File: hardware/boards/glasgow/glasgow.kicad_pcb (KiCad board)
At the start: 4 copper layers, 80 x 49 mm, 240 parts, among them J1 USB_B_Micro, J10 Conn_01x03, J2 Conn_02x10_Odd_Even, J3 Conn_02x10_Odd_Even, J4 Conn_01x02, J5 Conn_02x22_Odd_Even, J6 Conn_01x08, J7 Conn_01x08, J8 Conn_01x08, J9 Conn_01x08, U1 CY7C68013A-56LTX, U10 SN74LVC1T45DRL, U11 SN74LVC1T45DRL, U12 ADC081C021CIMM, U13 DAC081C081CIMK, U14 TPS73101DBV, U15 TPD3S014, U16 SN74LVC1T45DRL, U17 SN74LVC1T45DRL, U18 SN74LVC1T45DRL, U19 PCA6408APW, U2 CAT24M01W, U20 DAC081C081CIMK, U21 ADC081C021CIMM, U22 SN74LVC1T45DRL, U23 SN74LVC1T45DRL, U24 SN74LVC1T45DRL, U25 SN74LVC1T45DRL, U26 SN74LVC1T45DRL, U27 SN74LVC1T45DRL, U28 SN74LVC1T45DRL, U29 SN74LVC1T45DRL, U3 CAT24C256W, U30 ICE40HX8K-BG121, U31 TPS73101DBV, U32 SN74LVC1T45DRL, U33 MG2040, U34 ATECC508A, U35 MG2040, U36 TLV73312PQDRVRQ1, U4 SN74LVC1T45DRL, U5 PCA6408APW, U6 SN74LVC1T45DRL, U7 LM3880MF-1AF, U8 TLV75533PDRVR, U9 SN74LVC1T45DRL, Y1 24M

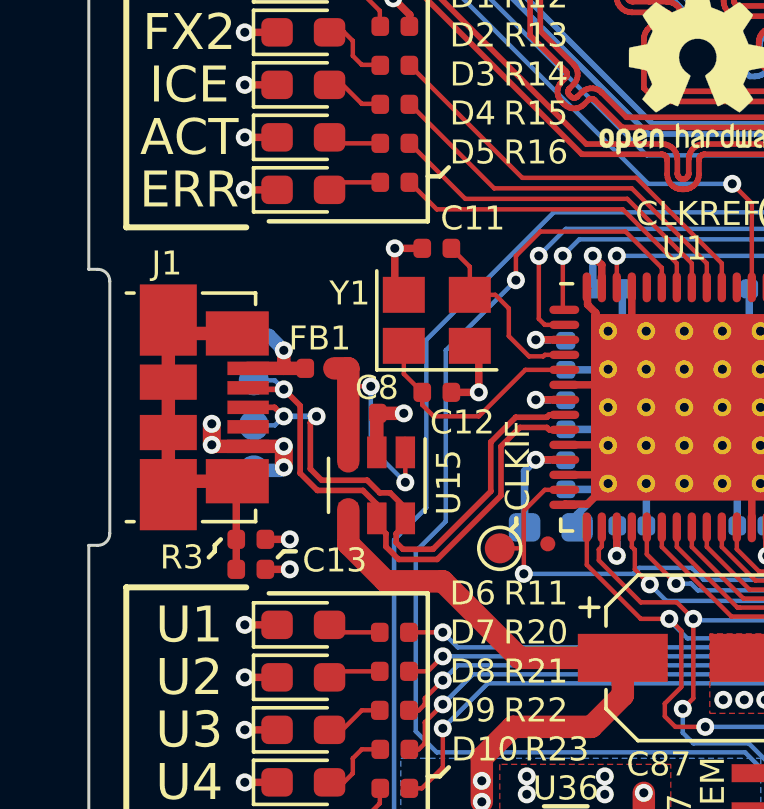
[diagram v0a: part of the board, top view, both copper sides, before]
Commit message: revC1-usbc: changed usb micro connector to usb type C
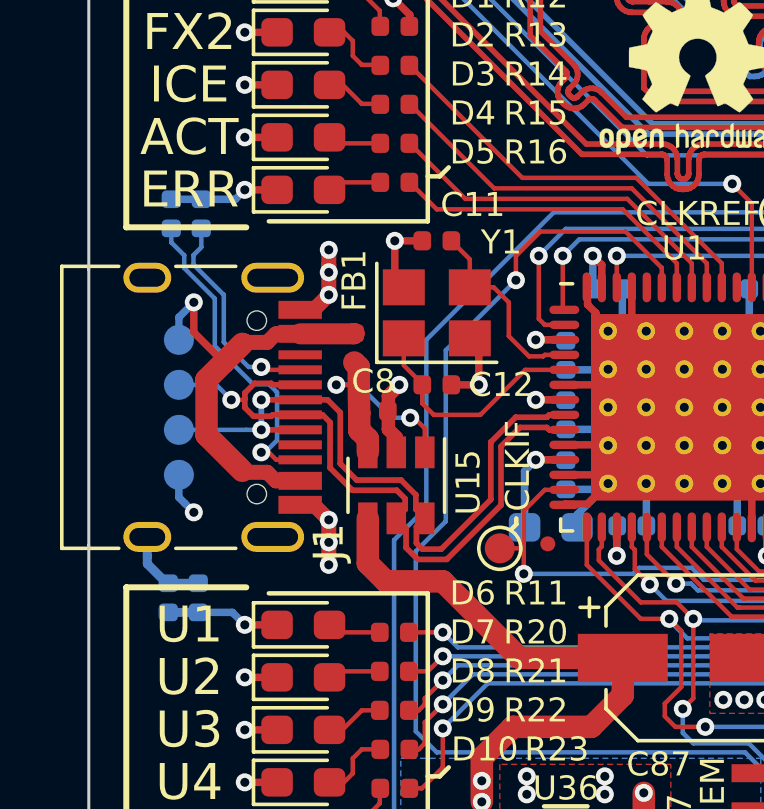
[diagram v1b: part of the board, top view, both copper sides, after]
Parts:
- added R52: 5k11, Resistor_SMD:R_0402_1005Metric, B.Cu at (53.8, 89.0)
- added R53: 5k11, Resistor_SMD:R_0402_1005Metric, B.Cu at (52.8, 89.0)
- C13, R3: moved to B.Cu
- J1: value USB_B_Micro -> USB_C_Receptacle_USB2.0; footprint Connector_USB:USB_Micro-B_Molex_47346-0001 -> Connector_USB:USB_C_Receptacle_HRO_TYPE-C-31-M-12
- moved R3 3.37 mm to (52.6, 101.8), turned to 270 degrees
- moved TP13 2.50 mm to (53.0, 93.3)
- moved TP14 2.50 mm to (53.0, 97.8)
- moved TP15 2.50 mm to (53.0, 96.3)
- moved TP16 2.50 mm to (53.0, 94.8)
- moved C13 1.99 mm to (53.6, 101.8), turned to 270 degrees
- moved FB1 1.34 mm to (58.9, 93.5), turned to 270 degrees
- moved J1 0.85 mm to (53.0, 95.5)
- moved U15 0.65 mm to (60.2, 98.1)
- moved C8 0.34 mm to (59.5, 95.6)
- moved C11 0.25 mm to (61.6, 90.0)
- moved C12 0.25 mm to (61.6, 94.8)
- moved Y1 0.25 mm to (61.6, 92.3)
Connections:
- FB1 pad 1: Net-(FB1-Pad1) -> /VUSBIN
- TP13 pad 1: Net-(FB1-Pad1) -> /VUSBIN
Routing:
- net /VUSBIN: track 0.00 -> 15.7 mm, vias 0 -> 1
- net /SHLD: track 15.1 -> 3.68 mm
- net /USB_CC2: track 0.00 -> 10.9 mm, vias 0 -> 1
- net /USB_CC1: track 0.00 -> 7.25 mm, vias 0 -> 1
- net GND: track 262.0 -> 267.1 mm, vias 116 -> 117
- net /USB_N: track 18.7 -> 22.8 mm
- net Net-(FB1-Pad1): track 3.71 -> 0.00 mm, vias 1 -> 0
- net /USB_P: track 18.9 -> 22.3 mm
- net /VUSB: track 9.50 -> 8.35 mm
- net +5V: track 167.8 -> 167.2 mm
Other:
- outline, holes or cut-outs redrawn

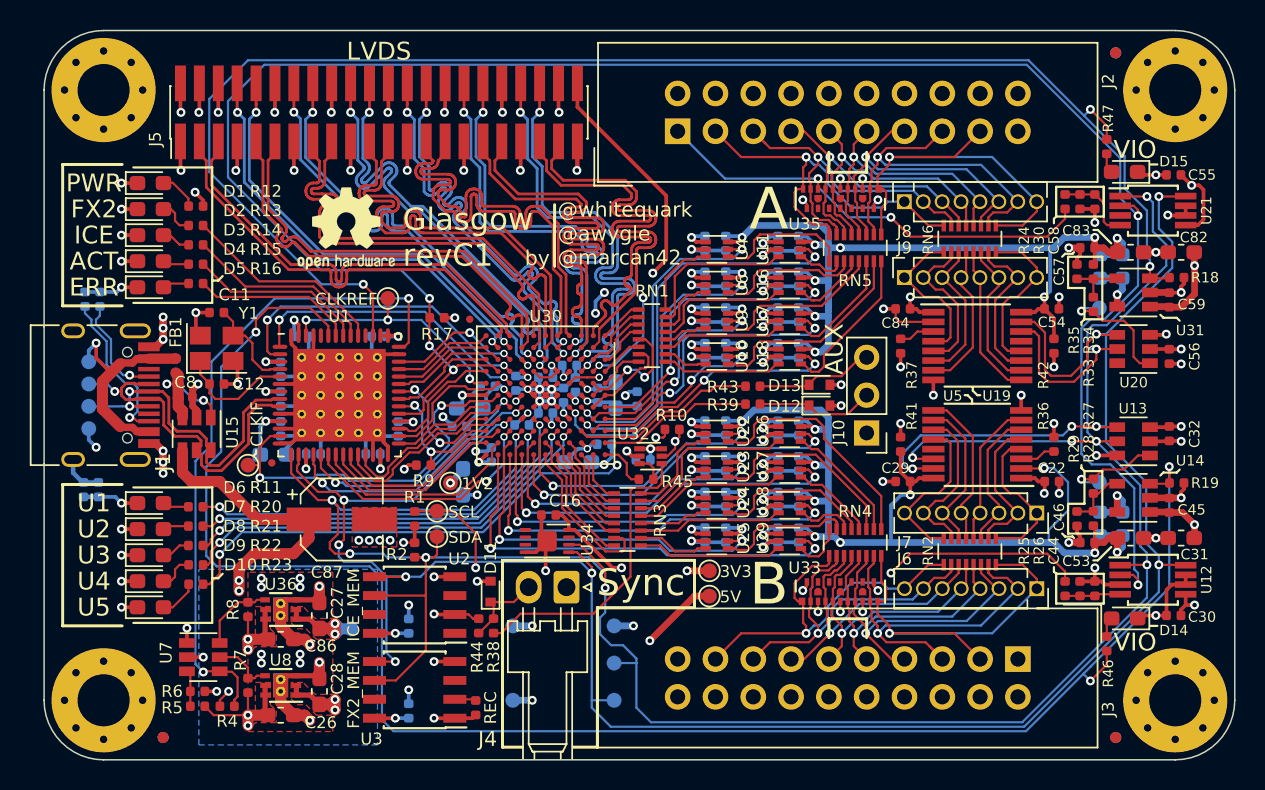
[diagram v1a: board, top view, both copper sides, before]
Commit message: changed level shifters, passing DRC
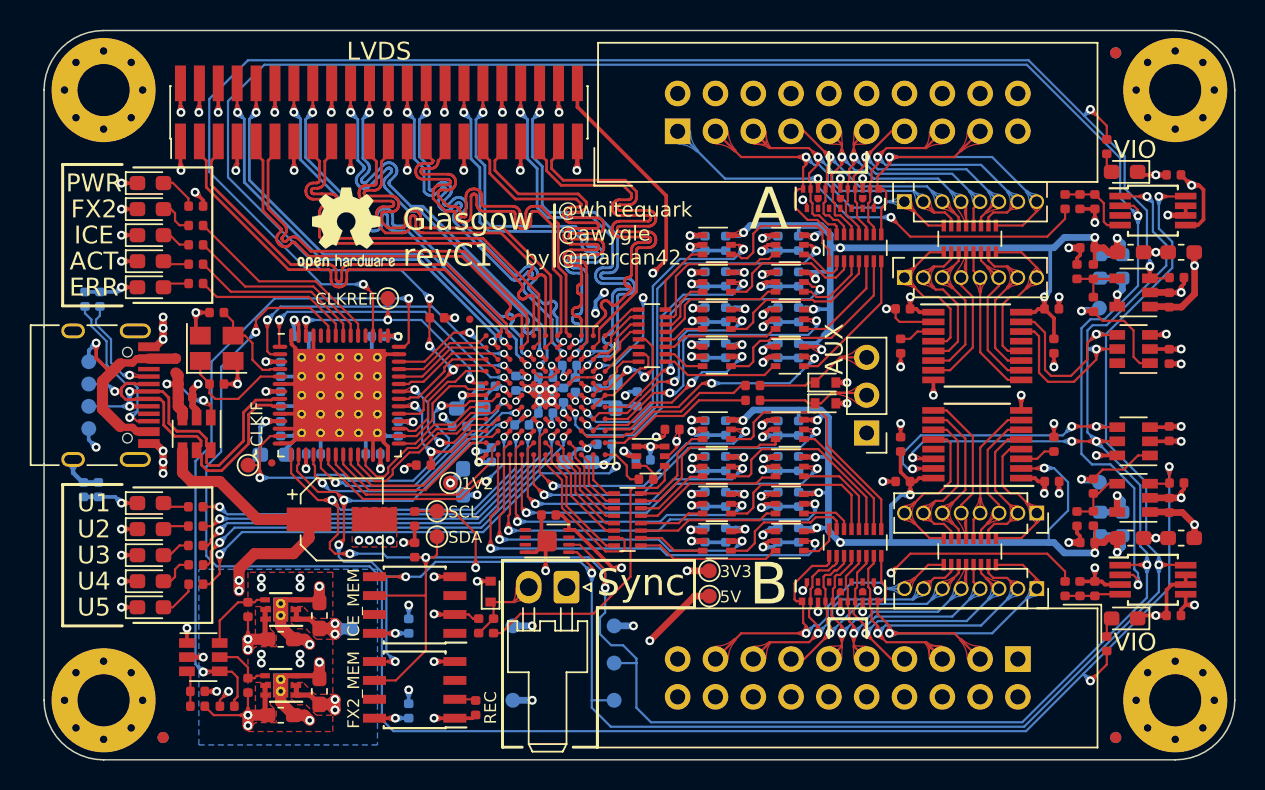
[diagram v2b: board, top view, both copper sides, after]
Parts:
- R52, R53: value 5k11 -> 5K1
- U10, U11, U16, U17, U18, U22, U23, U24, U25, U26, U27, U28, U29, U32, U4, U6, U9: footprint Glasgow:SOT-563 -> Package_TO_SOT_SMD:SOT-363_SC-70-6
- moved D12 0.43 mm to (102.5, 96.0)
- moved D13 0.43 mm to (102.5, 94.7)
- moved U11 0.30 mm to (100.1, 85.4)
- moved U22 0.30 mm to (95.2, 97.8)
- moved U26 0.30 mm to (100.1, 97.8)
- moved U4 0.30 mm to (95.2, 85.4)
- moved R39 0.25 mm to (97.6, 95.8)
- moved U23 0.20 mm to (95.2, 100.3)
- moved U27 0.20 mm to (100.1, 100.3)
- moved U16 0.20 mm to (100.1, 87.9)
- moved U6 0.20 mm to (95.2, 87.9)
- moved U24 0.10 mm to (95.2, 102.8)
- moved U28 0.10 mm to (100.1, 102.8)
- moved U17 0.10 mm to (100.1, 90.4)
- moved U9 0.10 mm to (95.2, 90.4)
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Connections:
- J1 pad A8: Net-(J1-PadA8) -> (no net)
- J1 pad B8: Net-(J1-PadB8) -> (no net)
- J2 pad 19: Net-(J2-Pad19) -> (no net)
- J2 pad 20: Net-(J2-Pad20) -> (no net)
- J3 pad 19: Net-(J3-Pad19) -> (no net)
- J3 pad 20: Net-(J3-Pad20) -> (no net)
- U1 pad 46: Net-(U1-Pad46) -> (no net)
- U1 pad 52: Net-(U1-Pad52) -> (no net)
- U19 pad 13: Net-(U19-Pad13) -> (no net)
- U2 pad 1: Net-(U2-Pad1) -> (no net)
- U2 pad 3: Net-(U2-Pad3) -> (no net)
- U2 pad 7: Net-(U2-Pad7) -> (no net)
- U20 pad 6: /IO_Banks/IO_Buffer_A/ADRDAC -> (no net)
- U21 pad 3: /IO_Banks/IO_Buffer_A/ADRADC -> (no net)
- U3 pad 3: Net-(U3-Pad3) -> (no net)
- U3 pad 7: Net-(U3-Pad7) -> (no net)
- U30 pad B10: Net-(U30-PadB10) -> (no net)
- U33 pad 13: Net-(U33-Pad13) -> (no net)
- U33 pad 14: Net-(U33-Pad14) -> (no net)
- U33 pad 15: Net-(U33-Pad15) -> (no net)
- U33 pad 16: Net-(U33-Pad16) -> (no net)
- U33 pad 17: Net-(U33-Pad17) -> (no net)
- U33 pad 19: Net-(U33-Pad19) -> (no net)
- U33 pad 20: Net-(U33-Pad20) -> (no net)
- U33 pad 21: Net-(U33-Pad21) -> (no net)
- U35 pad 13: Net-(U35-Pad13) -> (no net)
- U35 pad 14: Net-(U35-Pad14) -> (no net)
- U35 pad 15: Net-(U35-Pad15) -> (no net)
- U35 pad 16: Net-(U35-Pad16) -> (no net)
- U35 pad 17: Net-(U35-Pad17) -> (no net)
- U35 pad 19: Net-(U35-Pad19) -> (no net)
- U35 pad 20: Net-(U35-Pad20) -> (no net)
- U35 pad 21: Net-(U35-Pad21) -> (no net)
- U5 pad 13: Net-(U5-Pad13) -> (no net)
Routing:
- net +3V3: track 115.5 -> 112.3 mm
- net /IO_Banks/VIOB: track 114.0 -> 111.2 mm
- net GND: track 267.1 -> 265.1 mm
- net /IO_Banks/VIOA: track 103.6 -> 102.0 mm
- net /IO_Banks/IO_Buffer_B/Y4: track 10.8 -> 12.1 mm
- net /IO_Banks/IO_Buffer_A/Y0: track 9.26 -> 10.2 mm
- net /IO_Banks/IO_Buffer_B/Y7: track 3.71 -> 2.78 mm
- net /IO_Banks/IO_Buffer_B/Y3: track 5.64 -> 6.48 mm
- net /IO_Banks/IO_Buffer_A/Y7: track 10.6 -> 9.76 mm
- net /IO_Banks/IO_Buffer_A/Y5: track 7.77 -> 7.15 mm
- net /IO_Banks/DA3: track 20.7 -> 21.3 mm
- net /IO_Banks/IO_Buffer_B/Y0: track 16.3 -> 16.9 mm

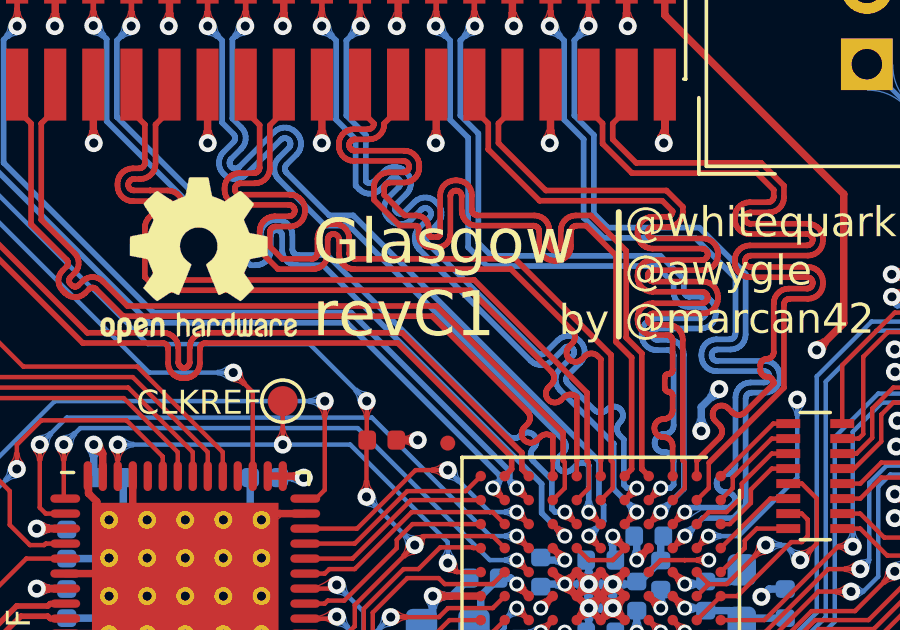
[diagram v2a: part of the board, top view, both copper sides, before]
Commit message: silk changes
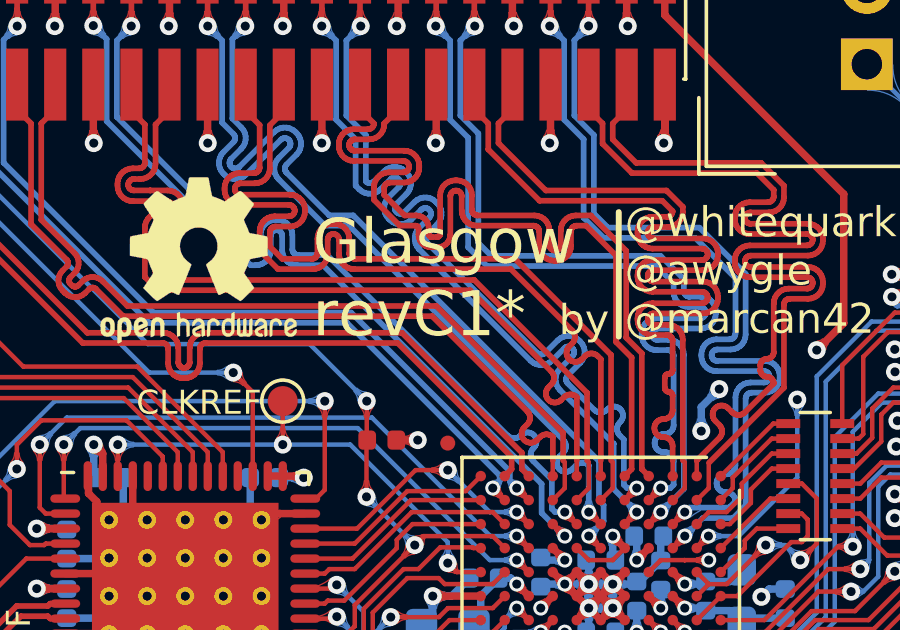
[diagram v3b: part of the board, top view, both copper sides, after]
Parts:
- removed NONO_HANA: MECHOKKU, Glasgow:nono_hana
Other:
- board text added: "Glasgow revC1*"
- board text removed: "Glasgow revC1"
- board text removed: "Serial No:"
